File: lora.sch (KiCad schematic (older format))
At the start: 58 parts, among them J1 Conn_01x02, J10 Conn, J11 Conn_Coaxial, J2 Humidity, J3 Temp, J4 Programming_Jumper, J5 Temp, J6 VDD, J7 GPS, J8 SIM800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

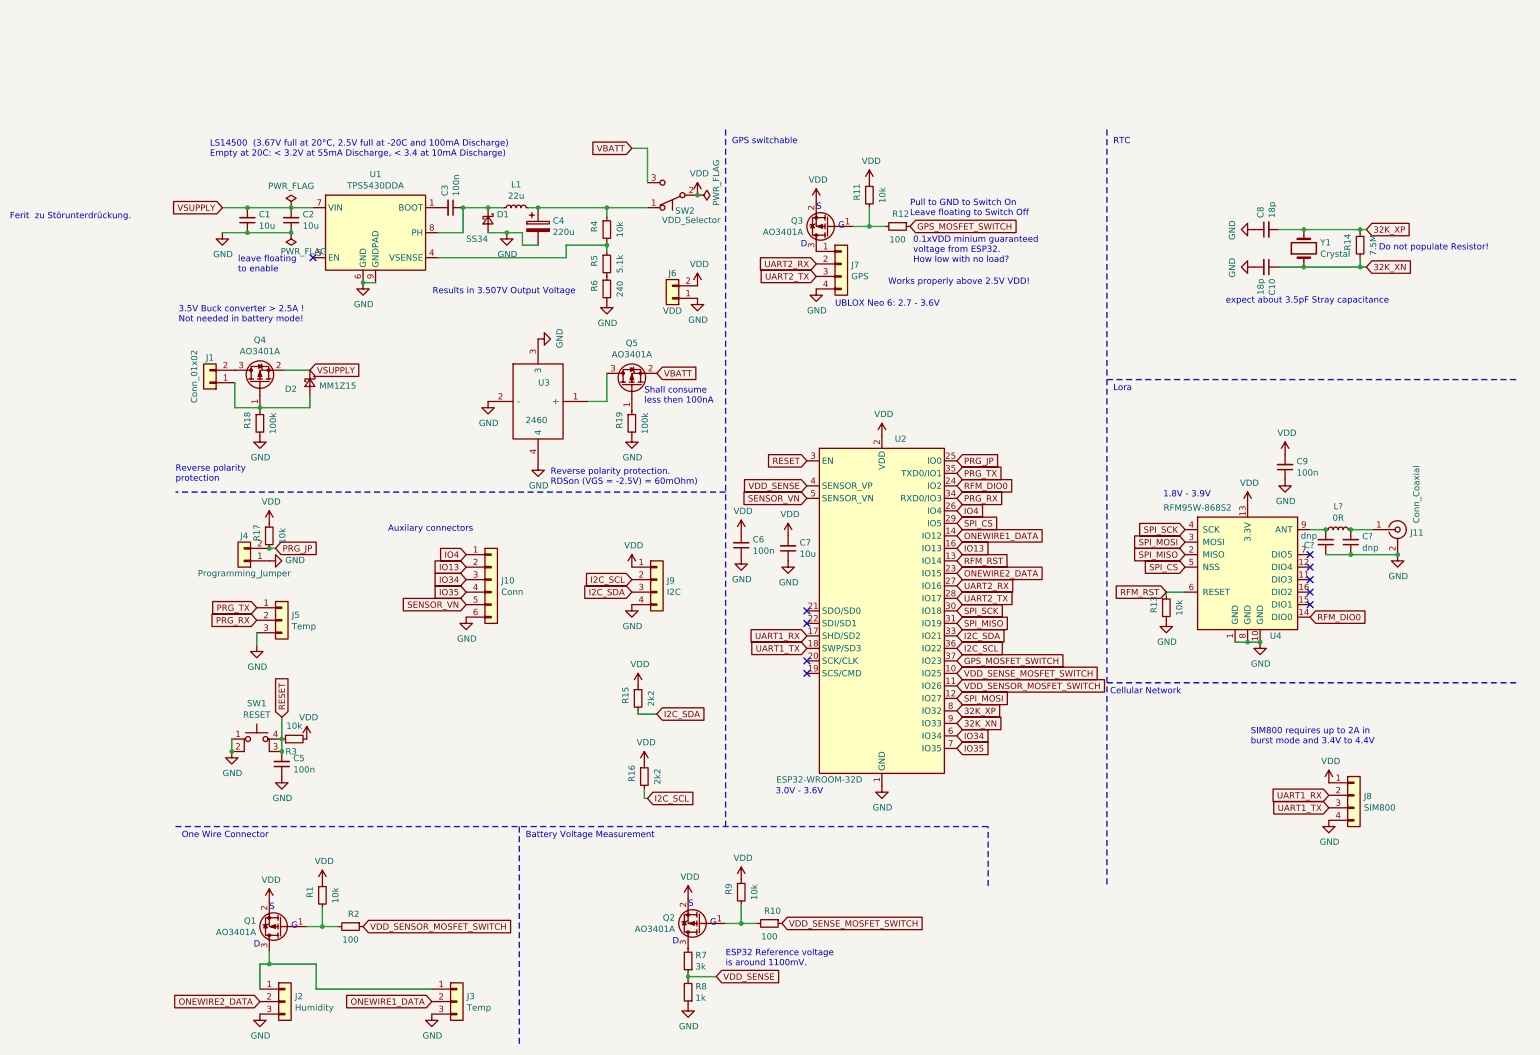
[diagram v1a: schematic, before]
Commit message: some progress with layout. Added ferrit bead to schematic.
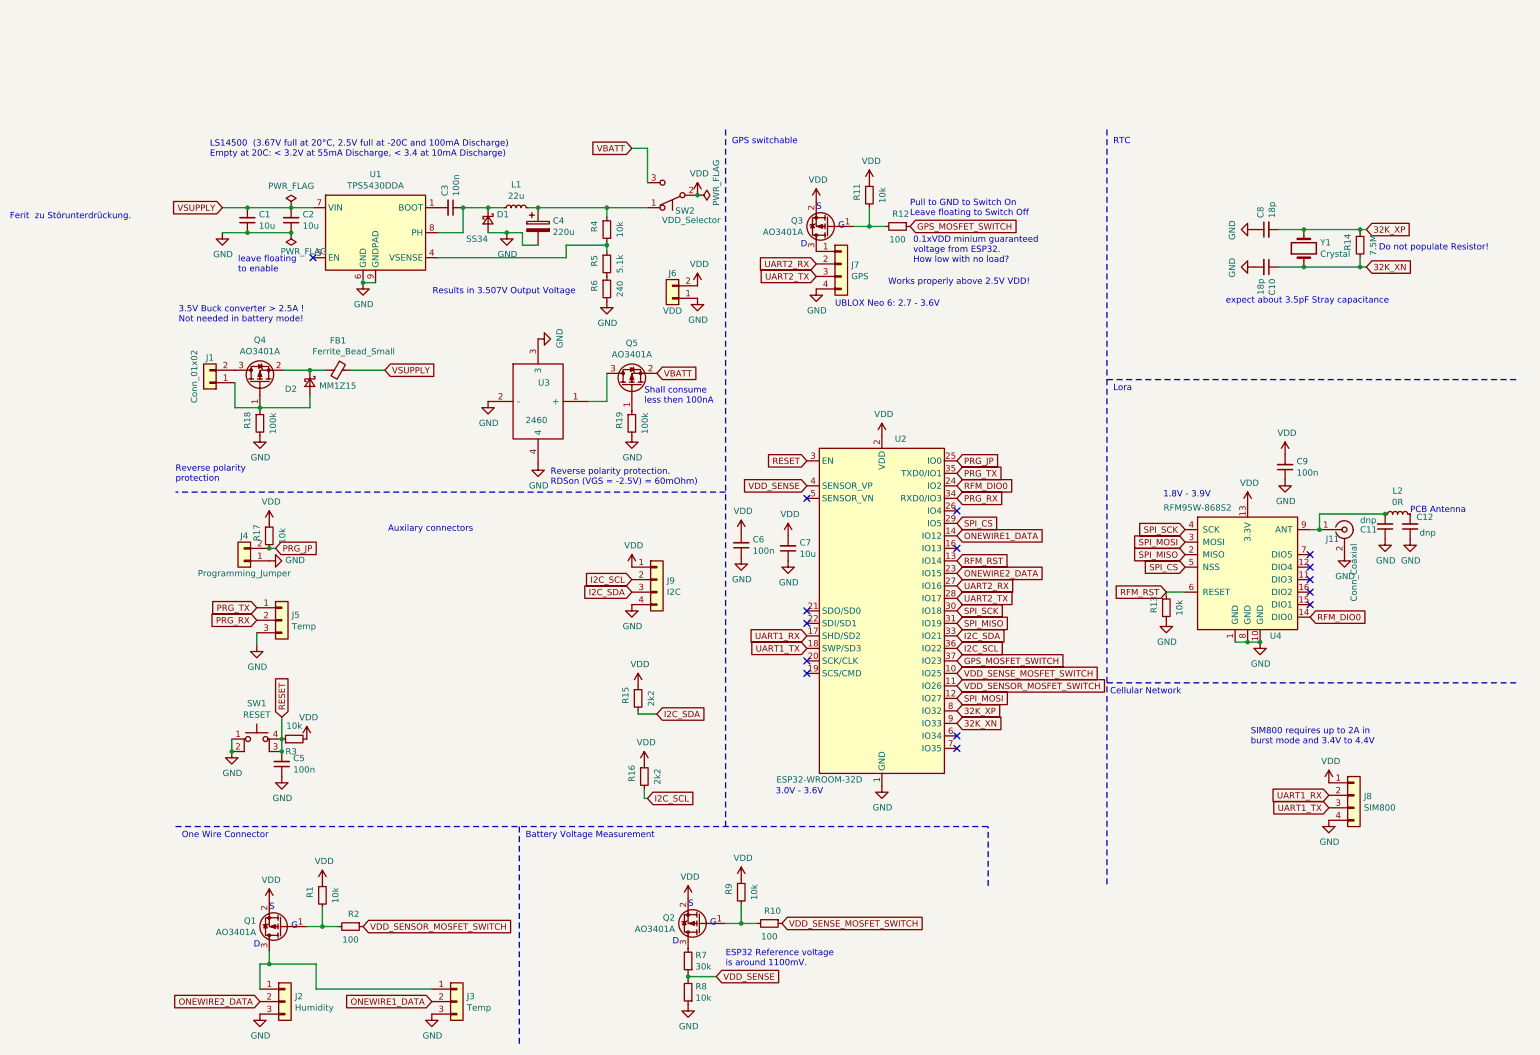
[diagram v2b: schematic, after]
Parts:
- removed J10: Conn, Connector_PinHeader_2.54mm:PinHeader_1x06_P2.54mm_Vertical, symbol Connector_Generic:Conn_01x06
- added FB1: Ferrite_Bead_Small, Resistor_SMD:R_0805_2012Metric, symbol Device:Ferrite_Bead_Small
- J11: footprint Connector_Coaxial:SMA_Amphenol_132134_Vertical -> Connector_Coaxial:SMA_Molex_73251-2120_EdgeMount_Horizontal
- R7: value 3k -> 30k; LCSC C4211 -> C22984
- R8: value 1k -> 10k; LCSC C21190 -> C25804
- U3: footprint 2460 -> SamacSys_Parts:2460
- gave numbers to parts that had none: 3
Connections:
- net VSUPPLY: now also FB1.1; no longer D2.1 (K), Q4.2 (S)
- net at C11.2, L2.1, U4.9 (ANT): now also J11.1 (In)
- net at C12.2, L2.2: no longer J11.1 (In)
- net IO13: no longer names the net of U2.16 (IO13)
- net IO34: no longer names the net of U2.6 (IO34)
- net IO35: no longer names the net of U2.7 (IO35)
- net IO4: no longer names the net of U2.26 (IO4)
- net SENSOR_VN: no longer names the net of U2.5 (SENSOR_VN)
- new net: D2.1 (K), FB1.2, Q4.2 (S)
- no-connect marks 10 -> 15
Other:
- note added: "PCB Antenna"
- moved on the sheet: C11, C12, J11, L2
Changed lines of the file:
@@
 P 4575 7125
 F 0 "R7" H 4516 7079 50  0000 R CNN
-F 1 "3k" H 4516 7170 50  0000 R CNN
+F 1 "30k" H 4516 7170 50  0000 R CNN
 F 2 "Resistor_SMD:R_0603_1608Metric" H 4575 7125 50  0001 C CNN
 F 3 "~" H 4575 7125 50  0001 C CNN
-F 4 "C4211" H 4575 7125 50  0001 C CNN "LCSC"
+F 4 "C22984" H 4575 7125 50  0001 C CNN "LCSC"
 	1    4575 7125
 	-1   0    0    1
@@
 P 4575 7375
 F 0 "R8" H 4516 7329 50  0000 R CNN
-F 1 "1k" H 4516 7420 50  0000 R CNN
+F 1 "10k" H 4516 7420 50  0000 R CNN
 F 2 "Resistor_SMD:R_0603_1608Metric" H 4575 7375 50  0001 C CNN
 F 3 "~" H 4575 7375 50  0001 C CNN
-F 4 "C21190" H 4575 7375 50  0001 C CNN "LCSC"
+F 4 "C25804" H 4575 7375 50  0001 C CNN "LCSC"
 	1    4575 7375
 	-1   0    0    1
@@
 	1275 3825 1225 3825
 Connection ~ 1225 3825
-Text GLabel 2800 3975 0    50   Input ~ 0
-IO13
-$Comp
-L Connector_Generic:Conn_01x06 J10
-U 1 1 5FC2A657
-P 3000 4075
-F 0 "J10" H 3080 4067 50  0000 L CNN
-F 1 "Conn" H 3080 3976 50  0000 L CNN
-F 2 "Connector_PinHeader_2.54mm:PinHeader_1x06_P2.54mm_Vertical" H 3000 4075 50  0001 C CNN
-F 3 "~" H 3000 4075 50  0001 C CNN
-	1    3000 4075
-	1    0    0    -1
-$EndComp
-$Comp
-L power:GND #PWR03
-U 1 1 5FC2BE00
-P 2800 4375
-F 0 "#PWR03" H 2800 4125 50  0001 C CNN
-F 1 "GND" H 2805 4202 50  0000 C CNN
-F 2 "" H 2800 4375 50  0001 C CNN
-F 3 "" H 2800 4375 50  0001 C CNN
-	1    2800 4375
-	1    0    0    -1
-$EndComp
-Text GLabel 2800 4275 0    50   Input ~ 0
-SENSOR_VN
 $Comp
 L power:PWR_FLAG #FLG0101
@@
 L Connector:Conn_Coaxial J11
 U 1 1 5FC31EE2
-P 10250 3675
-F 0 "J11" H 10350 3650 50  0000 L CNN
-F 1 "Conn_Coaxial" V 10400 3725 50  0000 L CNN
-F 2 "Connector_Coaxial:SMA_Amphenol_132134_Vertical" H 10250 3675 50  0001 C CNN
-F 3 " ~" H 10250 3675 50  0001 C CNN
-	1    10250 3675
+P 9825 3675
+F 0 "J11" H 9675 3600 50  0000 L CNN
+F 1 "Conn_Coaxial" V 9900 3100 50  0000 L CNN
+F 2 "Connector_Coaxial:SMA_Molex_73251-2120_EdgeMount_Horizontal" H 9825 3675 50  0001 C CNN
+F 3 " ~" H 9825 3675 50  0001 C CNN
+	1    9825 3675
 	1    0    0    -1
 $EndComp
@@
 L power:GND #PWR0146
 U 1 1 5FC3451D
-P 10250 3875
-F 0 "#PWR0146" H 10250 3625 50  0001 C CNN
-F 1 "GND" H 10255 3702 50  0000 C CNN
-F 2 "" H 10250 3875 50  0001 C CNN
-F 3 "" H 10250 3875 50  0001 C CNN
-	1    10250 3875
+P 9825 3875
+F 0 "#PWR0146" H 9825 3625 50  0001 C CNN
+F 1 "GND" H 9830 3702 50  0000 C CNN
+F 2 "" H 9825 3875 50  0001 C CNN
+F 3 "" H 9825 3875 50  0001 C CNN
+	1    9825 3875
 	1    0    0    -1
 $EndComp
@@
 Text Notes 8875 1875 0    50   ~ 0
 expect about 3.5pF Stray capacitance
-Text GLabel 2800 3875 0    50   Input ~ 0
-IO4
-Text GLabel 2800 4075 0    50   Input ~ 0
-IO34
-Text GLabel 2800 4175 0    50   Input ~ 0
-IO35
 Wire Notes Line
 	4875 475  4875 6050
-Text Notes 2175 3700 0    50   ~ 0
-Auxilary connectors
 $Comp
 L power:PWR_FLAG #FLG0102
@@
 Text GLabel 850  1100 0    50   Input ~ 0
 VSUPPLY
-Text GLabel 1550 2400 2    50   Input ~ 0
+Text GLabel 2150 2400 2    50   Input ~ 0
 VSUPPLY
 Wire Wire Line
@@
 F 0 "U3" H 3375 2800 50  0000 L CNN
 F 1 "2460" H 3275 2500 50  0000 L CNN
-F 2 "2460" H 3625 2950 50  0001 L CNN
+F 2 "SamacSys_Parts:2460" H 3625 2950 50  0001 L CNN
 F 3 "http://www.keyelco.com/product-pdf.cfm?p=1025" H 3625 2850 50  0001 L CNN
 F 4 "Battery Holder; AA; Polypropylene; PC Mount; 1; Spring; PC Lug" H 3625 2750 50  0001 L CNN "Description"
@@
 	1    0    0    -1
 $EndComp
-Text GLabel 6725 5425 2    50   Input ~ 0
-IO35
-Text GLabel 6725 5325 2    50   Input ~ 0
-IO34
-Text GLabel 6725 3525 2    50   Input ~ 0
-IO4
 Text GLabel 6725 5225 2    50   Input ~ 0
 32K_XN
 Text GLabel 6725 5125 2    50   Input ~ 0
 32K_XP
-Text GLabel 5525 3425 0    50   Input ~ 0
-SENSOR_VN
-Text GLabel 6725 3825 2    50   Input ~ 0
-IO13
 NoConn ~ 5525 4325
 NoConn ~ 5525 4425
@@
 Shall consume \nless then 100nA
 $Comp
-L Device:C_Small C?
+L Device:C_Small C12
 U 1 1 5FC2AFEC
-P 9875 3775
-F 0 "C?" H 9783 3729 50  0000 R CNN
-F 1 "dnp" H 9783 3820 50  0000 R CNN
-F 2 "Capacitor_SMD:C_0603_1608Metric" H 9875 3775 50  0001 C CNN
-F 3 "~" H 9875 3775 50  0001 C CNN
-F 4 "" H 9875 3775 50  0001 C CNN "LCSC"
-	1    9875 3775
+P 10350 3650
+F 0 "C12" H 10300 3575 50  0000 R CNN
+F 1 "dnp" H 10275 3700 50  0000 R CNN
+F 2 "Capacitor_SMD:C_0603_1608Metric" H 10350 3650 50  0001 C CNN
+F 3 "~" H 10350 3650 50  0001 C CNN
+F 4 "" H 10350 3650 50  0001 C CNN "LCSC"
+	1    10350 3650
 	-1   0    0    1
 $EndComp
@@
 	8550 4175 8400 4175
 $Comp
-L Device:L_Small L?
+L Device:L_Small L2
 U 1 1 5FC42B81
-P 9775 3675
-F 0 "L?" V 9960 3675 50  0000 C CNN
-F 1 "0R" V 9869 3675 50  0000 C CNN
-F 2 "Resistor_SMD:R_0603_1608Metric" H 9775 3675 50  0001 C CNN
-F 3 "~" H 9775 3675 50  0001 C CNN
-F 4 "C21189" V 9775 3675 50  0001 C CNN "LCSC"
-	1    9775 3675
+P 10250 3550
+F 0 "L2" V 10435 3550 50  0000 C CNN
+F 1 "0R" V 10344 3550 50  0000 C CNN
+F 2 "Resistor_SMD:R_0603_1608Metric" H 10250 3550 50  0001 C CNN
+F 3 "~" H 10250 3550 50  0001 C CNN
+F 4 "C21189" V 10250 3550 50  0001 C CNN "LCSC"
+	1    10250 3550
 	0    -1   -1   0
 $EndComp
 $Comp
-L Device:C_Small C?
+L Device:C_Small C11
 U 1 1 5FC4504E
-P 9675 3775
-F 0 "C?" H 9850 3800 50  0000 R CNN
-F 1 "dnp" H 9875 3725 50  0000 R CNN
-F 2 "Capacitor_SMD:C_0603_1608Metric" H 9675 3775 50  0001 C CNN
-F 3 "~" H 9675 3775 50  0001 C CNN
-F 4 "" H 9675 3775 50  0001 C CNN "LCSC"
-	1    9675 3775
+P 10150 3650
+F 0 "C11" H 10350 3675 50  0000 R CNN
+F 1 "dnp" H 10350 3600 50  0000 R CNN
+F 2 "Capacitor_SMD:C_0603_1608Metric" H 10150 3650 50  0001 C CNN
+F 3 "~" H 10150 3650 50  0001 C CNN
+F 4 "" H 10150 3650 50  0001 C CNN "LCSC"
+	1    10150 3650
 	-1   0    0    1
 $EndComp
-Wire Wire Line
-	9550 3675 9675 3675
-Connection ~ 9675 3675
-Wire Wire Line
-	9875 3675 10050 3675
-Connection ~ 9875 3675
-Wire Wire Line
-	10250 3875 9875 3875
-Connection ~ 10250 3875
-Wire Wire Line
-	9875 3875 9675 3875
-Connection ~ 9875 3875
 Text Notes -850 1200 0    50   ~ 0
 Ferit  zu Störunterdrückung.
+Text Notes 2175 3700 0    50   ~ 0
+Auxilary connectors
+NoConn ~ 6725 3525
+NoConn ~ 6725 3825
+NoConn ~ 6725 5325
+NoConn ~ 6725 5425
+NoConn ~ 5525 3425
+$Comp
+L Device:Ferrite_Bead_Small FB1
+U 1 1 5FCB2F22
+P 1775 2400
+F 0 "FB1" V 1538 2400 50  0000 C CNN
+F 1 "Ferrite_Bead_Small" V 1625 2525 50  0000 C CNN
+F 2 "Resistor_SMD:R_0805_2012Metric" V 1705 2400 50  0001 C CNN
+F 3 "~" H 1775 2400 50  0001 C CNN
+F 4 "C1017" H 1775 2400 50  0001 C CNN "LCSC"
+	1    1775 2400
+	0    1    1    0
+$EndComp
+Connection ~ 1550 2400
+Wire Wire Line
+	1550 2400 1675 2400
+Wire Wire Line
+	1875 2400 2150 2400
+Wire Wire Line
+	9550 3675 9625 3675
+Wire Wire Line
+	9625 3675 9625 3550
+Wire Wire Line
+	9625 3550 10150 3550
+Connection ~ 9625 3675
+Connection ~ 10150 3550
+$Comp
+L power:GND #PWR0148
+U 1 1 5FD64FE0
+P 10150 3750
+F 0 "#PWR0148" H 10150 3500 50  0001 C CNN
+F 1 "GND" H 10155 3577 50  0000 C CNN
+F 2 "" H 10150 3750 50  0001 C CNN
+F 3 "" H 10150 3750 50  0001 C CNN
+	1    10150 3750
+	1    0    0    -1
+$EndComp
+$Comp
+L power:GND #PWR0149
+U 1 1 5FD65447
+P 10350 3750
+F 0 "#PWR0149" H 10350 3500 50  0001 C CNN
+F 1 "GND" H 10355 3577 50  0000 C CNN
+F 2 "" H 10350 3750 50  0001 C CNN
+F 3 "" H 10350 3750 50  0001 C CNN
+	1    10350 3750
+	1    0    0    -1
+$EndComp
+Text Notes 10350 3550 0    50   ~ 0
+PCB Antenna
 $EndSCHEMATC

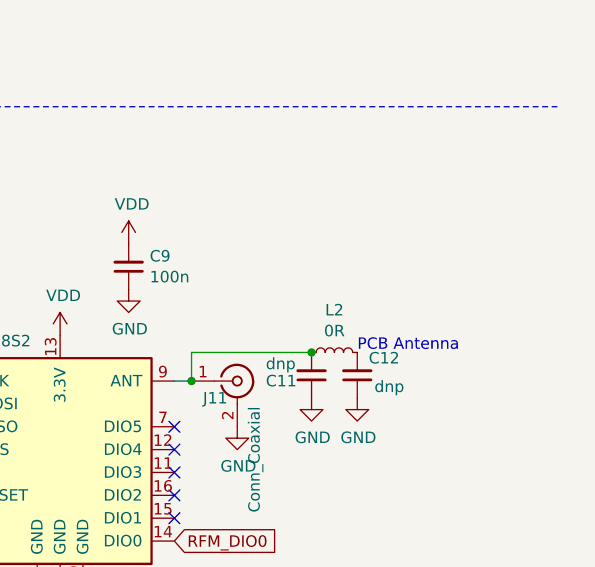
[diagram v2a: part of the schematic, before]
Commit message: added cutouts for antenna.
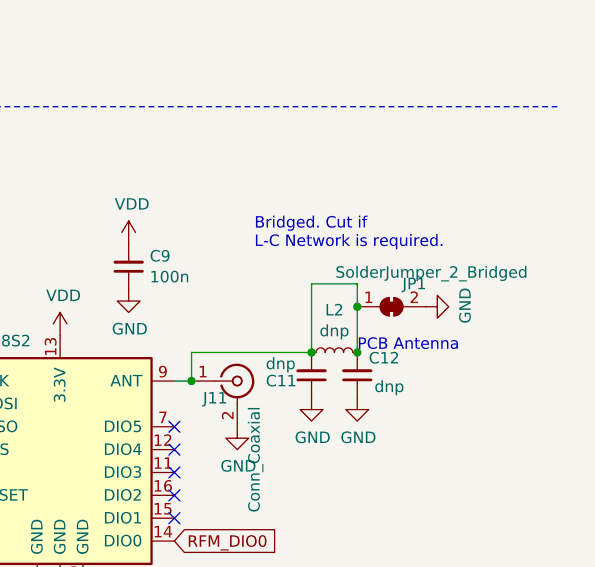
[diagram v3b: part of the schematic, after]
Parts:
- added JP1: SolderJumper_2_Bridged, Jumper:SolderJumper-2_P1.3mm_Bridged_Pad1.0x1.5mm, symbol Jumper:SolderJumper_2_Bridged
- L2: value 0R -> dnp
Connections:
- net GND: now also JP1.2 (B)
- net at C11.2, J11.1 (In), L2.1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: now also C12.2, L2.2, JP1.1 (A)
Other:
- note added: "Bridged. Cut if \nL-C Network is required."
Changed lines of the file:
@@
 P 10250 3550
 F 0 "L2" V 10435 3550 50  0000 C CNN
-F 1 "0R" V 10344 3550 50  0000 C CNN
+F 1 "dnp" V 10344 3550 50  0000 C CNN
 F 2 "Resistor_SMD:R_0603_1608Metric" H 10250 3550 50  0001 C CNN
 F 3 "~" H 10250 3550 50  0001 C CNN
@@
 Text Notes 10350 3550 0    50   ~ 0
 PCB Antenna
+Wire Wire Line
+	10150 3550 10150 3250
+Wire Wire Line
+	10150 3250 10350 3250
+Wire Wire Line
+	10350 3250 10350 3350
+Connection ~ 10350 3550
+Text Notes 9900 3100 0    50   ~ 0
+Bridged. Cut if \nL-C Network is required.
+$Comp
+L Jumper:SolderJumper_2_Bridged JP1
+U 1 1 5FDC7049
+P 10500 3350
+F 0 "JP1" H 10600 3450 50  0000 C CNN
+F 1 "SolderJumper_2_Bridged" H 10675 3500 50  0000 C CNN
+F 2 "Jumper:SolderJumper-2_P1.3mm_Bridged_Pad1.0x1.5mm" H 10500 3350 50  0001 C CNN
+F 3 "~" H 10500 3350 50  0001 C CNN
+	1    10500 3350
+	1    0    0    -1
+$EndComp
+Connection ~ 10350 3350
+Wire Wire Line
+	10350 3350 10350 3550
+$Comp
+L power:GND #PWR02
+U 1 1 5FDC9B31
+P 10650 3350
+F 0 "#PWR02" H 10650 3100 50  0001 C CNN
+F 1 "GND" H 10655 3177 50  0000 C CNN
+F 2 "" H 10650 3350 50  0001 C CNN
+F 3 "" H 10650 3350 50  0001 C CNN
+	1    10650 3350
+	0    -1   -1   0
+$EndComp
 $EndSCHEMATC

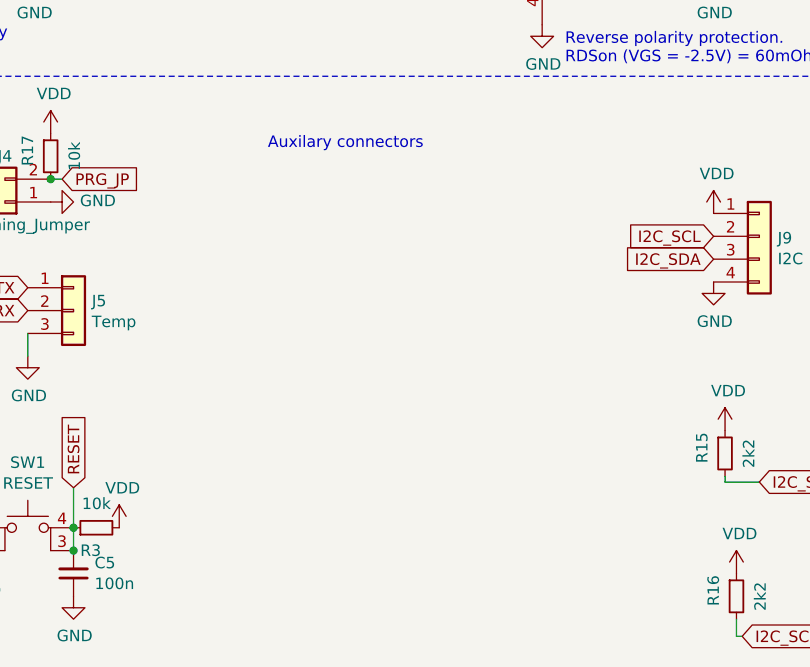
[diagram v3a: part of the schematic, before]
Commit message: added mounting holes for GPS
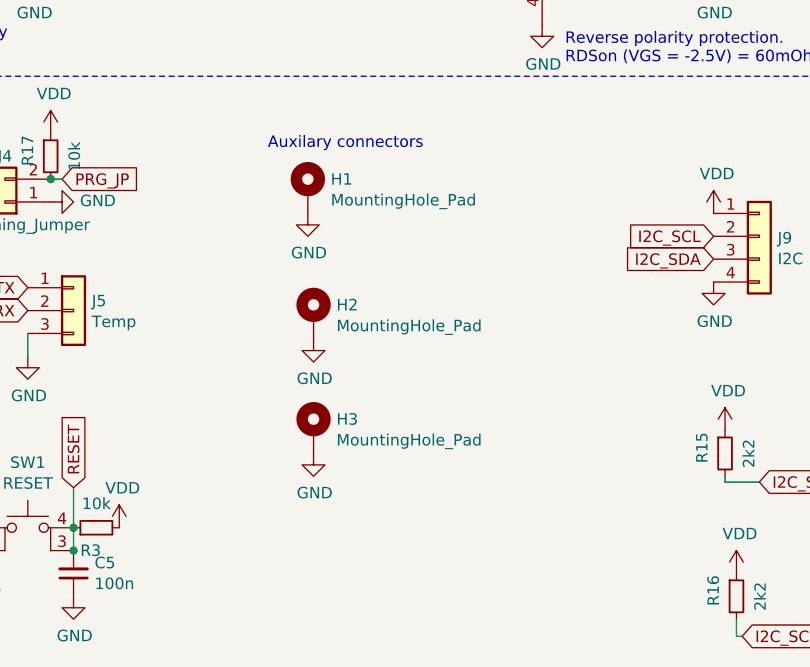
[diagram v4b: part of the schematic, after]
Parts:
- added H1, H2, H3: MountingHole_Pad, MountingHole:MountingHole_2.2mm_M2_DIN965_Pad, symbol Mechanical:MountingHole_Pad
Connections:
- net GND: now also H1.1, H2.1, H3.1
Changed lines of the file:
@@
 	0    -1   -1   0
 $EndComp
+$Comp
+L Mechanical:MountingHole_Pad H1
+U 1 1 5FE846A8
+P 2350 3875
+F 0 "H1" H 2450 3924 50  0000 L CNN
+F 1 "MountingHole_Pad" H 2450 3833 50  0000 L CNN
+F 2 "MountingHole:MountingHole_2.2mm_M2_DIN965_Pad" H 2350 3875 50  0001 C CNN
+F 3 "~" H 2350 3875 50  0001 C CNN
+	1    2350 3875
+	1    0    0    -1
+$EndComp
+$Comp
+L power:GND #PWR03
+U 1 1 5FE8619C
+P 2350 3975
+F 0 "#PWR03" H 2350 3725 50  0001 C CNN
+F 1 "GND" H 2355 3802 50  0000 C CNN
+F 2 "" H 2350 3975 50  0001 C CNN
+F 3 "" H 2350 3975 50  0001 C CNN
+	1    2350 3975
+	1    0    0    -1
+$EndComp
+$Comp
+L Mechanical:MountingHole_Pad H2
+U 1 1 5FEA1D5A
+P 2375 4425
+F 0 "H2" H 2475 4474 50  0000 L CNN
+F 1 "MountingHole_Pad" H 2475 4383 50  0000 L CNN
+F 2 "MountingHole:MountingHole_2.2mm_M2_DIN965_Pad" H 2375 4425 50  0001 C CNN
+F 3 "~" H 2375 4425 50  0001 C CNN
+	1    2375 4425
+	1    0    0    -1
+$EndComp
+$Comp
+L power:GND #PWR04
+U 1 1 5FEA1D60
+P 2375 4525
+F 0 "#PWR04" H 2375 4275 50  0001 C CNN
+F 1 "GND" H 2380 4352 50  0000 C CNN
+F 2 "" H 2375 4525 50  0001 C CNN
+F 3 "" H 2375 4525 50  0001 C CNN
+	1    2375 4525
+	1    0    0    -1
+$EndComp
+$Comp
+L Mechanical:MountingHole_Pad H3
+U 1 1 5FED213B
+P 2375 4925
+F 0 "H3" H 2475 4974 50  0000 L CNN
+F 1 "MountingHole_Pad" H 2475 4883 50  0000 L CNN
+F 2 "MountingHole:MountingHole_2.2mm_M2_DIN965_Pad" H 2375 4925 50  0001 C CNN
+F 3 "~" H 2375 4925 50  0001 C CNN
+	1    2375 4925
+	1    0    0    -1
+$EndComp
+$Comp
+L power:GND #PWR05
+U 1 1 5FED2141
+P 2375 5025
+F 0 "#PWR05" H 2375 4775 50  0001 C CNN
+F 1 "GND" H 2380 4852 50  0000 C CNN
+F 2 "" H 2375 5025 50  0001 C CNN
+F 3 "" H 2375 5025 50  0001 C CNN
+	1    2375 5025
+	1    0    0    -1
+$EndComp
 $EndSCHEMATC

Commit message: minor things
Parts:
- L2: value dnp -> 0R
- R14: value 7.5M -> dnp
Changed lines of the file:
@@
 P 9950 1400
 F 0 "R14" V 9850 1425 50  0000 C CNN
-F 1 "7.5M" V 10055 1400 50  0000 C CNN
+F 1 "dnp" V 10055 1400 50  0000 C CNN
 F 2 "Resistor_SMD:R_0603_1608Metric" H 9950 1400 50  0001 C CNN
 F 3 "~" H 9950 1400 50  0001 C CNN
@@
 P 10250 3550
 F 0 "L2" V 10435 3550 50  0000 C CNN
-F 1 "dnp" V 10344 3550 50  0000 C CNN
+F 1 "0R" V 10344 3550 50  0000 C CNN
 F 2 "Resistor_SMD:R_0603_1608Metric" H 10250 3550 50  0001 C CNN
 F 3 "~" H 10250 3550 50  0001 C CNN
